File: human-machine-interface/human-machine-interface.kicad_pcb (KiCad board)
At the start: 2 copper layers, 86.4 x 47 mm, 26 parts, among them J1 Conn_01x04_Male, J2 Conn_01x04_Male, J3 Conn_01x04_Male, J4 Conn_01x04_Male, J5 5.4mm/2.5mm, SW1 SW_Push, SW2 SW_Push, SW3 SW_DPDT_x2, U1 NRF24L01+, U2 Teensy3.2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

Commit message: Finish HMI PCB
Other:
- board text added: "Maarten De Munck Vijfendertig BVBA"
- board text added: "RC Volvo C202 HMI Rev. 1 (20200612)"

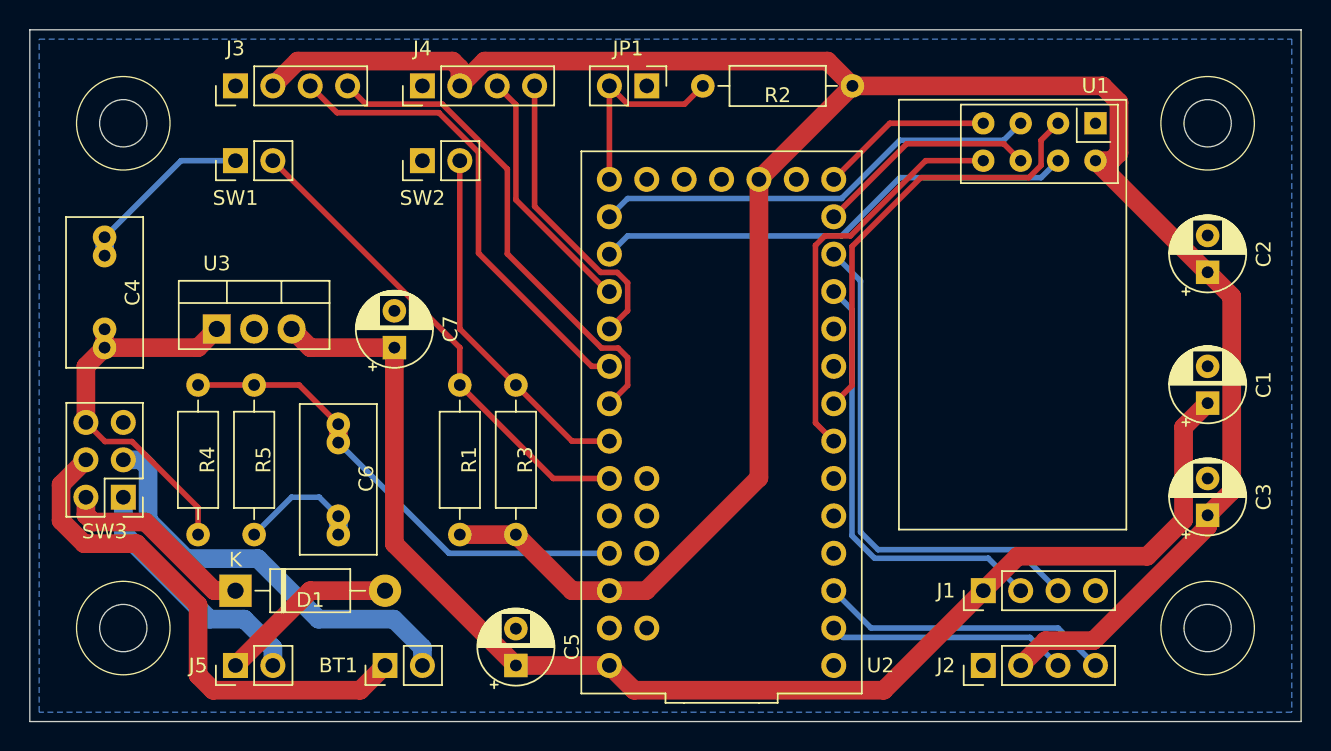
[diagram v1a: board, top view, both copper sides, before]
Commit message: Use proper mounting holes
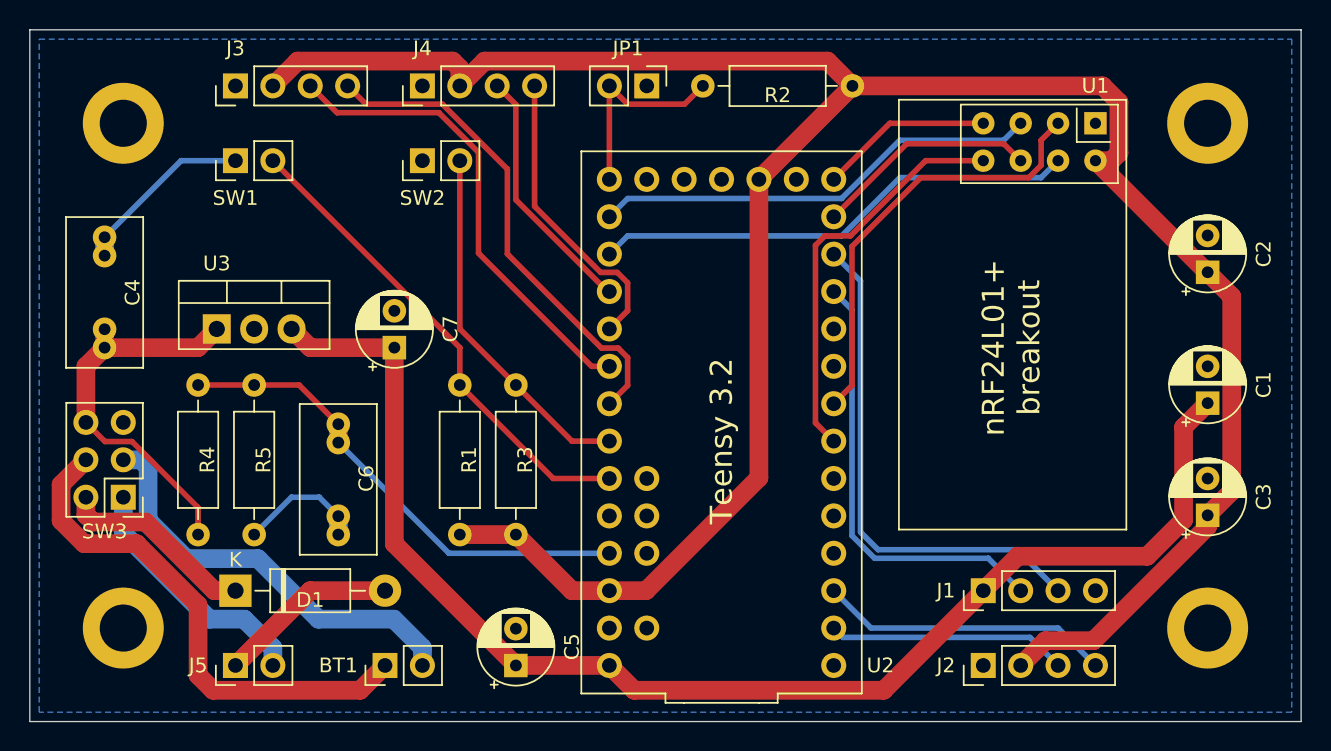
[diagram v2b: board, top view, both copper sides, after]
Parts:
- added REF**: MountingHole_3.2mm_M3_ISO14580_Pad, MountingHole:MountingHole_3.2mm_M3_ISO14580_Pad, F.Cu at (146.1, 130.8)
- added REF**: MountingHole_3.2mm_M3_ISO14580_Pad, MountingHole:MountingHole_3.2mm_M3_ISO14580_Pad, F.Cu at (146.1, 165.1)
- added REF**: MountingHole_3.2mm_M3_ISO14580_Pad, MountingHole:MountingHole_3.2mm_M3_ISO14580_Pad, F.Cu at (72.4, 165.1)
- added REF**: MountingHole_3.2mm_M3_ISO14580_Pad, MountingHole:MountingHole_3.2mm_M3_ISO14580_Pad, F.Cu at (72.4, 130.8)
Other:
- outline, holes or cut-outs redrawn
- board text added: "Teensy 3.2"
- board text added: "nRF24L01+ breakout"
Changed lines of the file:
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@@
   (general
     (thickness 1.6)
-    (drawings 14)
+    (drawings 8)
     (tracks 176)
     (zones 0)
-    (modules 26)
+    (modules 30)
     (nets 41)
   )
@@
     (add_net "Net-(U2-Pad6)")
     (add_net "Net-(U2-Pad9)")
+  )
+  (module MountingHole:MountingHole_3.2mm_M3_ISO14580_Pad (layer F.Cu)
+    (at 146.05 130.81)
+    (descr "Mounting Hole 3.2mm, M3, ISO14580")
+    (tags "mounting hole 3.2mm m3 iso14580")
+    (attr virtual)
+    (fp_text reference REF** (at 0 -3.75) (layer F.SilkS) hide
+      (effects (font (size 1 1) (thickness 0.15)))
+    )
+    (fp_text value MountingHole_3.2mm_M3_ISO14580_Pad (at 0 3.75) (layer F.Fab) hide
+      (effects (font (size 1 1) (thickness 0.15)))
+    )
+    (fp_circle (center 0 0) (end 2.75 0) (layer Cmts.User) (width 0.15))
+    (fp_circle (center 0 0) (end 3 0) (layer F.CrtYd) (width 0.05))
+    (fp_text user %R (at 0.3 0) (layer F.Fab) hide
+      (effects (font (size 1 1) (thickness 0.15)))
+    )
+    (pad 1 thru_hole circle (at 0 0) (size 5.5 5.5) (drill 3.2) (layers *.Cu *.Mask))
+  )
+  (module MountingHole:MountingHole_3.2mm_M3_ISO14580_Pad (layer F.Cu)
+    (at 146.05 165.1)
+    (descr "Mounting Hole 3.2mm, M3, ISO14580")
+    (tags "mounting hole 3.2mm m3 iso14580")
+    (attr virtual)
+    (fp_text reference REF** (at 0 -3.75) (layer F.SilkS) hide
+      (effects (font (size 1 1) (thickness 0.15)))
+    )
+    (fp_text value MountingHole_3.2mm_M3_ISO14580_Pad (at 0 3.75) (layer F.Fab) hide
+      (effects (font (size 1 1) (thickness 0.15)))
+    )
+    (fp_circle (center 0 0) (end 2.75 0) (layer Cmts.User) (width 0.15))
+    (fp_circle (center 0 0) (end 3 0) (layer F.CrtYd) (width 0.05))
+    (fp_text user %R (at 0.3 0) (layer F.Fab) hide
+      (effects (font (size 1 1) (thickness 0.15)))
+    )
+    (pad 1 thru_hole circle (at 0 0) (size 5.5 5.5) (drill 3.2) (layers *.Cu *.Mask))
+  )
+  (module MountingHole:MountingHole_3.2mm_M3_ISO14580_Pad (layer F.Cu)
+    (at 72.39 165.1)
+    (descr "Mounting Hole 3.2mm, M3, ISO14580")
+    (tags "mounting hole 3.2mm m3 iso14580")
+    (attr virtual)
+    (fp_text reference REF** (at 0 -3.75) (layer F.SilkS) hide
+      (effects (font (size 1 1) (thickness 0.15)))
+    )
+    (fp_text value MountingHole_3.2mm_M3_ISO14580_Pad (at 0 3.75) (layer F.Fab) hide
+      (effects (font (size 1 1) (thickness 0.15)))
+    )
+    (fp_text user %R (at 0.3 0) (layer F.Fab) hide
+      (effects (font (size 1 1) (thickness 0.15)))
+    )
+    (fp_circle (center 0 0) (end 2.75 0) (layer Cmts.User) (width 0.15))
+    (fp_circle (center 0 0) (end 3 0) (layer F.CrtYd) (width 0.05))
+    (pad 1 thru_hole circle (at 0 0) (size 5.5 5.5) (drill 3.2) (layers *.Cu *.Mask))
+  )
+  (module MountingHole:MountingHole_3.2mm_M3_ISO14580_Pad (layer F.Cu)
+    (at 72.39 130.81)
+    (descr "Mounting Hole 3.2mm, M3, ISO14580")
+    (tags "mounting hole 3.2mm m3 iso14580")
+    (attr virtual)
+    (fp_text reference REF** (at 0 -3.75) (layer F.SilkS) hide
+      (effects (font (size 1 1) (thickness 0.15)))
+    )
+    (fp_text value MountingHole_3.2mm_M3_ISO14580_Pad (at 0 3.75) (layer F.Fab) hide
+      (effects (font (size 1 1) (thickness 0.15)))
+    )
+    (fp_text user %R (at 0.3 0) (layer F.Fab) hide
+      (effects (font (size 1 1) (thickness 0.15)))
+    )
+    (fp_circle (center 0 0) (end 2.75 0) (layer Cmts.User) (width 0.15))
+    (fp_circle (center 0 0) (end 3 0) (layer F.CrtYd) (width 0.05))
+    (pad 1 thru_hole circle (at 0 0) (size 5.5 5.5) (drill 3.2) (layers *.Cu *.Mask))
   )
   (module Resistor_THT:R_Axial_DIN0207_L6.3mm_D2.5mm_P10.16mm_Horizontal (layer F.Cu)
@@
     )
   )
+  (gr_text "nRF24L01+\nbreakout" (at 132.715 146.05 90) (layer F.SilkS)
+    (effects (font (size 1.5 1.5) (thickness 0.15)))
+  )
+  (gr_text "Teensy 3.2" (at 113.03 152.4 90) (layer F.SilkS)
+    (effects (font (size 1.5 1.5) (thickness 0.15)))
+  )
   (gr_text "Maarten De Munck\nVijfendertig BVBA" (at 88.265 138.43) (layer B.SilkS)
     (effects (font (size 2 2) (thickness 0.2)) (justify mirror))
@@
   (gr_line (start 66.04 171.45) (end 152.4 171.45) (layer Edge.Cuts) (width 0.05))
   (gr_line (start 66.04 171.45) (end 66.04 124.46) (layer Edge.Cuts) (width 0.05))
-  (gr_circle (center 72.39 130.81) (end 73.914 130.302) (layer Edge.Cuts) (width 0.05))
-  (gr_circle (center 72.39 165.1) (end 73.914 164.592) (layer Edge.Cuts) (width 0.05))
-  (gr_circle (center 146.05 165.1) (end 147.574 164.592) (layer Edge.Cuts) (width 0.05))
-  (gr_circle (center 146.05 130.81) (end 147.574 130.302) (layer Edge.Cuts) (width 0.05))
-  (gr_circle (center 146.05 165.1) (end 149.225 165.1) (layer F.SilkS) (width 0.05))
-  (gr_circle (center 146.05 130.81) (end 149.225 130.81) (layer F.SilkS) (width 0.05))
-  (gr_circle (center 72.39 165.1) (end 75.565 165.1) (layer F.SilkS) (width 0.05))
-  (gr_circle (center 72.39 130.81) (end 75.565 130.81) (layer F.SilkS) (width 0.05))
   (segment (start 85.09 146.05) (end 83.82 144.78) (width 1.27) (layer F.Cu) (net 1))
   (segment (start 90.805 146.05) (end 85.09 146.05) (width 1.27) (layer F.Cu) (net 1))

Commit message: Use larger holes for nRF24L01+ breakout board
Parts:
- U1: footprint RF_Module:nRF24L01_Breakout -> earth-rover-footprints:nRF24L01_Breakout_LargerHoles

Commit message: Update human machine interface to KiCad 6.0
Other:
- net class Default removed
